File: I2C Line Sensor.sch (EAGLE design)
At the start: 28 parts, among them U1 ADS7830

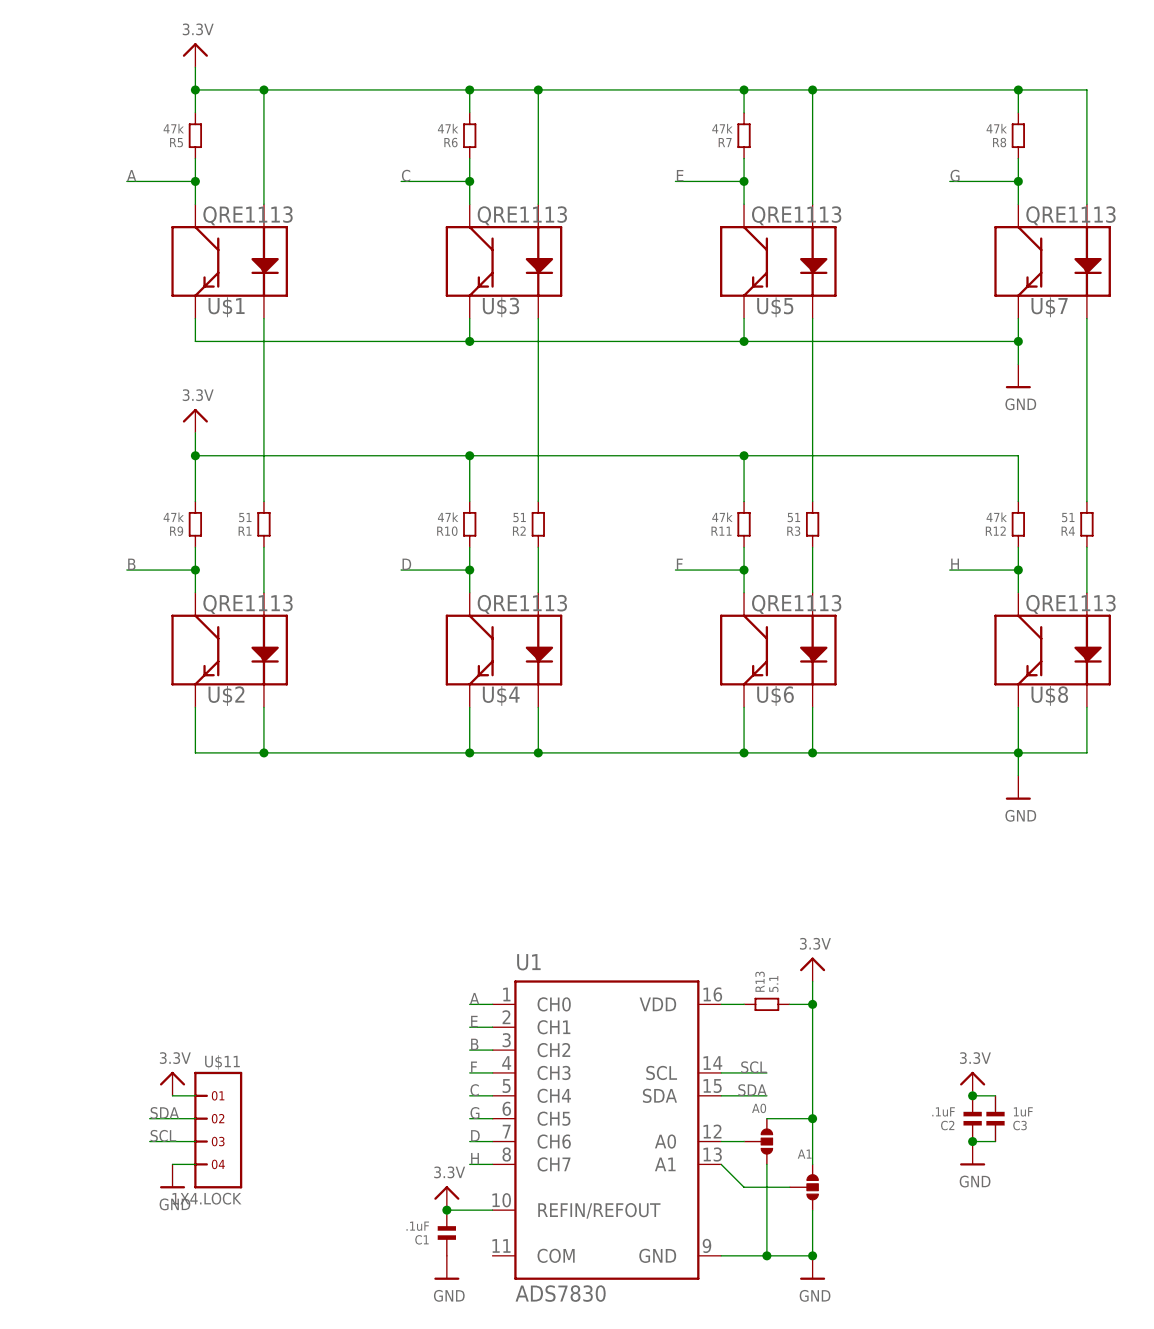
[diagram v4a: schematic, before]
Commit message: Modified resistor values such that the PCBs should no longer get hot
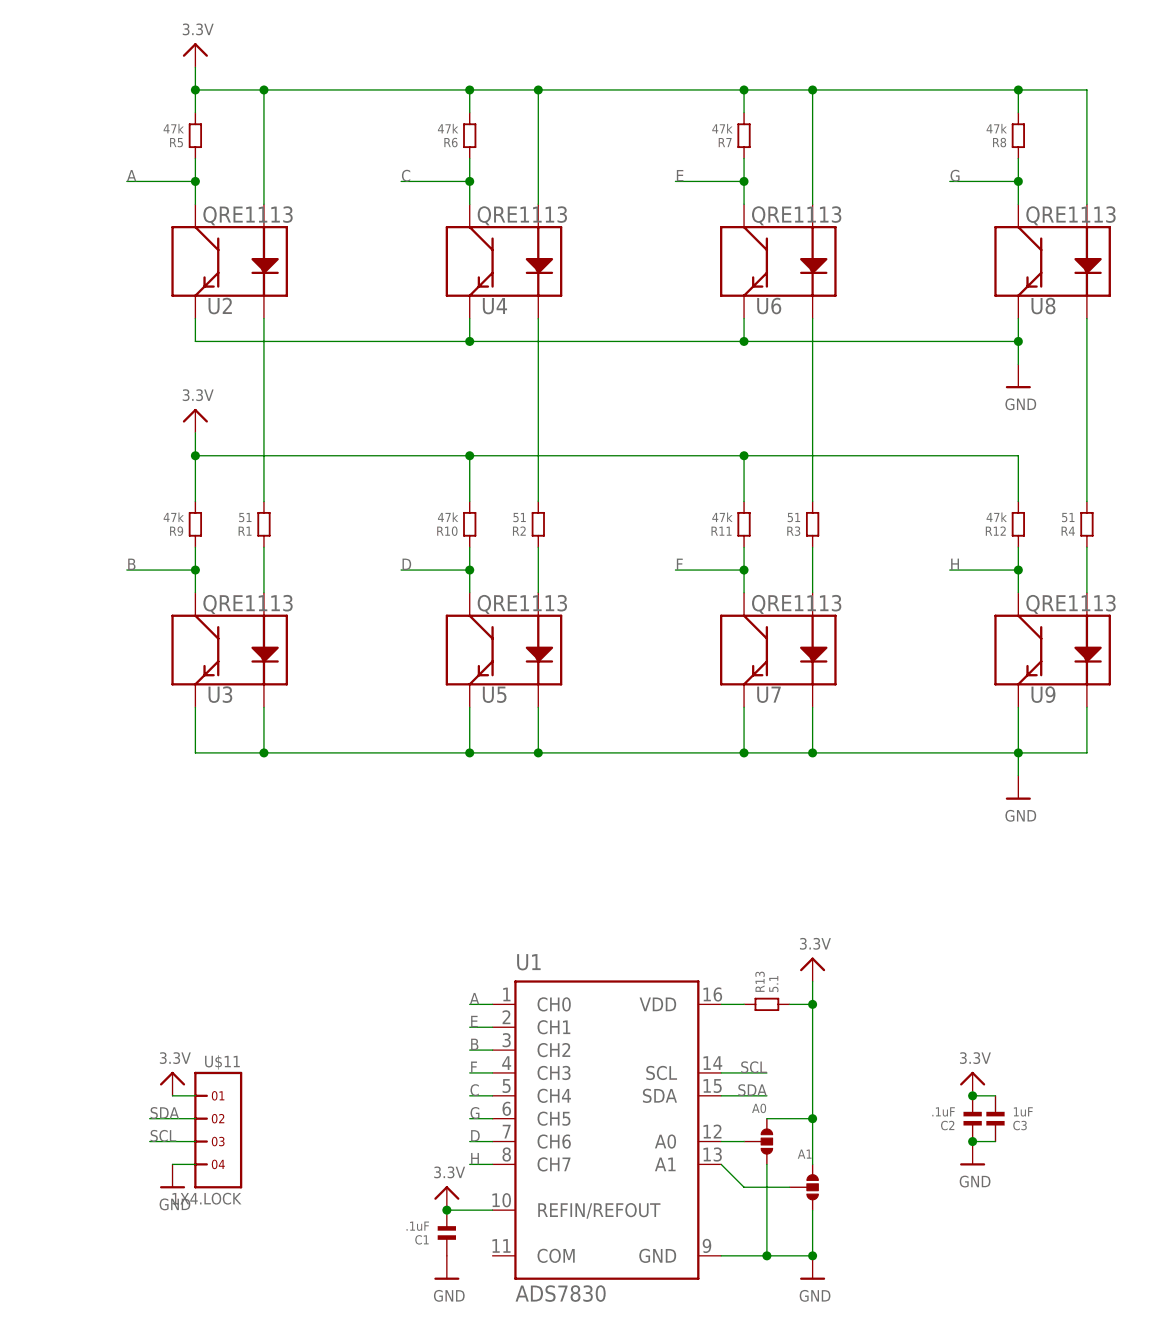
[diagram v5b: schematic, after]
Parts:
- renumbered U$1 to U2, U$2 to U3, U$3 to U4, U$4 to U5, U$5 to U6, U$6 to U7, U$7 to U8, U$8 to U9
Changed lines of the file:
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@@
 </classes>
 <parts>
-<part name="U$1" library="SparkFun" deviceset="QRE1113" device=""/>
-<part name="U$2" library="SparkFun" deviceset="QRE1113" device=""/>
-<part name="U$3" library="SparkFun" deviceset="QRE1113" device=""/>
-<part name="U$4" library="SparkFun" deviceset="QRE1113" device=""/>
-<part name="U$5" library="SparkFun" deviceset="QRE1113" device=""/>
-<part name="U$6" library="SparkFun" deviceset="QRE1113" device=""/>
-<part name="U$7" library="SparkFun" deviceset="QRE1113" device=""/>
-<part name="U$8" library="SparkFun" deviceset="QRE1113" device=""/>
+<part name="U2" library="SparkFun" deviceset="QRE1113" device=""/>
+<part name="U3" library="SparkFun" deviceset="QRE1113" device=""/>
+<part name="U4" library="SparkFun" deviceset="QRE1113" device=""/>
+<part name="U5" library="SparkFun" deviceset="QRE1113" device=""/>
+<part name="U6" library="SparkFun" deviceset="QRE1113" device=""/>
+<part name="U7" library="SparkFun" deviceset="QRE1113" device=""/>
+<part name="U8" library="SparkFun" deviceset="QRE1113" device=""/>
+<part name="U9" library="SparkFun" deviceset="QRE1113" device=""/>
 <part name="U1" library="burr-brown" deviceset="ADS7828" device="" value="ADS7830"/>
 <part name="U$14" library="microbuilder" deviceset="3.3V" device=""/>
@@
 </plain>
 <instances>
-<instance part="U$1" gate="G$1" x="27.94" y="144.78"/>
-<instance part="U$2" gate="G$1" x="27.94" y="101.6"/>
-<instance part="U$3" gate="G$1" x="58.42" y="144.78"/>
-<instance part="U$4" gate="G$1" x="58.42" y="101.6"/>
-<instance part="U$5" gate="G$1" x="88.9" y="144.78"/>
-<instance part="U$6" gate="G$1" x="88.9" y="101.6"/>
-<instance part="U$7" gate="G$1" x="119.38" y="144.78"/>
-<instance part="U$8" gate="G$1" x="119.38" y="101.6"/>
+<instance part="U2" gate="G$1" x="27.94" y="144.78"/>
+<instance part="U3" gate="G$1" x="27.94" y="101.6"/>
+<instance part="U4" gate="G$1" x="58.42" y="144.78"/>
+<instance part="U5" gate="G$1" x="58.42" y="101.6"/>
+<instance part="U6" gate="G$1" x="88.9" y="144.78"/>
+<instance part="U7" gate="G$1" x="88.9" y="101.6"/>
+<instance part="U8" gate="G$1" x="119.38" y="144.78"/>
+<instance part="U9" gate="G$1" x="119.38" y="101.6"/>
 <instance part="U1" gate="G$1" x="71.12" y="48.26"/>
 <instance part="U$14" gate="G$1" x="93.98" y="63.5"/>
@@
 <segment>
 <wire x1="33.02" y1="137.16" x2="33.02" y2="116.84" width="0.1524" layer="91"/>
-<pinref part="U$1" gate="G$1" pin="K"/>
+<pinref part="U2" gate="G$1" pin="K"/>
 <pinref part="R1" gate="G$1" pin="2"/>
 </segment>
@@
 <net name="N$3" class="0">
 <segment>
-<pinref part="U$2" gate="G$1" pin="A"/>
+<pinref part="U3" gate="G$1" pin="A"/>
 <pinref part="R1" gate="G$1" pin="1"/>
 <wire x1="33.02" y1="106.68" x2="33.02" y2="111.76" width="0.1524" layer="91"/>
@@
 <net name="N$4" class="0">
 <segment>
-<pinref part="U$4" gate="G$1" pin="A"/>
+<pinref part="U5" gate="G$1" pin="A"/>
 <pinref part="R2" gate="G$1" pin="1"/>
 <wire x1="63.5" y1="111.76" x2="63.5" y2="106.68" width="0.1524" layer="91"/>
@@
 <segment>
 <wire x1="63.5" y1="137.16" x2="63.5" y2="116.84" width="0.1524" layer="91"/>
-<pinref part="U$3" gate="G$1" pin="K"/>
+<pinref part="U4" gate="G$1" pin="K"/>
 <pinref part="R2" gate="G$1" pin="2"/>
 </segment>
@@
 <segment>
 <wire x1="93.98" y1="137.16" x2="93.98" y2="116.84" width="0.1524" layer="91"/>
-<pinref part="U$5" gate="G$1" pin="K"/>
+<pinref part="U6" gate="G$1" pin="K"/>
 <pinref part="R3" gate="G$1" pin="2"/>
 </segment>
@@
 <net name="N$7" class="0">
 <segment>
-<pinref part="U$6" gate="G$1" pin="A"/>
+<pinref part="U7" gate="G$1" pin="A"/>
 <pinref part="R3" gate="G$1" pin="1"/>
 <wire x1="93.98" y1="111.76" x2="93.98" y2="106.68" width="0.1524" layer="91"/>
@@
 <segment>
 <wire x1="124.46" y1="137.16" x2="124.46" y2="116.84" width="0.1524" layer="91"/>
-<pinref part="U$7" gate="G$1" pin="K"/>
+<pinref part="U8" gate="G$1" pin="K"/>
 <pinref part="R4" gate="G$1" pin="2"/>
 </segment>
@@
 <net name="N$9" class="0">
 <segment>
-<pinref part="U$8" gate="G$1" pin="A"/>
+<pinref part="U9" gate="G$1" pin="A"/>
 <pinref part="R4" gate="G$1" pin="1"/>
 <wire x1="124.46" y1="111.76" x2="124.46" y2="106.68" width="0.1524" layer="91"/>
@@
 <junction x="86.36" y="88.9"/>
 <junction x="116.84" y="88.9"/>
-<pinref part="U$2" gate="G$1" pin="K"/>
-<pinref part="U$8" gate="G$1" pin="K"/>
-<pinref part="U$4" gate="G$1" pin="K"/>
-<pinref part="U$6" gate="G$1" pin="K"/>
-<pinref part="U$4" gate="G$1" pin="E"/>
-<pinref part="U$6" gate="G$1" pin="E"/>
-<pinref part="U$2" gate="G$1" pin="E"/>
-<pinref part="U$8" gate="G$1" pin="E"/>
+<pinref part="U3" gate="G$1" pin="K"/>
+<pinref part="U9" gate="G$1" pin="K"/>
+<pinref part="U5" gate="G$1" pin="K"/>
+<pinref part="U7" gate="G$1" pin="K"/>
+<pinref part="U5" gate="G$1" pin="E"/>
+<pinref part="U7" gate="G$1" pin="E"/>
+<pinref part="U3" gate="G$1" pin="E"/>
+<pinref part="U9" gate="G$1" pin="E"/>
 <pinref part="U$22" gate="G$1" pin="GND"/>
 <wire x1="116.84" y1="86.36" x2="116.84" y2="88.9" width="0.1524" layer="91"/>
 </segment>
 <segment>
-<pinref part="U$7" gate="G$1" pin="E"/>
+<pinref part="U8" gate="G$1" pin="E"/>
 <wire x1="116.84" y1="134.62" x2="116.84" y2="137.16" width="0.1524" layer="91"/>
-<pinref part="U$5" gate="G$1" pin="E"/>
+<pinref part="U6" gate="G$1" pin="E"/>
 <wire x1="86.36" y1="134.62" x2="86.36" y2="137.16" width="0.1524" layer="91"/>
 <wire x1="86.36" y1="134.62" x2="116.84" y2="134.62" width="0.1524" layer="91"/>
 <junction x="86.36" y="134.62"/>
 <wire x1="55.88" y1="134.62" x2="86.36" y2="134.62" width="0.1524" layer="91"/>
-<pinref part="U$3" gate="G$1" pin="E"/>
+<pinref part="U4" gate="G$1" pin="E"/>
 <wire x1="55.88" y1="137.16" x2="55.88" y2="134.62" width="0.1524" layer="91"/>
 <junction x="55.88" y="134.62"/>
-<pinref part="U$1" gate="G$1" pin="E"/>
+<pinref part="U2" gate="G$1" pin="E"/>
 <wire x1="25.4" y1="137.16" x2="25.4" y2="134.62" width="0.1524" layer="91"/>
 <wire x1="25.4" y1="134.62" x2="55.88" y2="134.62" width="0.1524" layer="91"/>
@@
 <wire x1="25.4" y1="152.4" x2="25.4" y2="149.86" width="0.1524" layer="91"/>
 <wire x1="25.4" y1="152.4" x2="17.78" y2="152.4" width="0.1524" layer="91"/>
-<pinref part="U$1" gate="G$1" pin="C"/>
+<pinref part="U2" gate="G$1" pin="C"/>
 <pinref part="R5" gate="G$1" pin="1"/>
 <wire x1="25.4" y1="154.94" x2="25.4" y2="152.4" width="0.1524" layer="91"/>
@@
 <wire x1="25.4" y1="109.22" x2="25.4" y2="106.68" width="0.1524" layer="91"/>
 <wire x1="25.4" y1="109.22" x2="17.78" y2="109.22" width="0.1524" layer="91"/>
-<pinref part="U$2" gate="G$1" pin="C"/>
+<pinref part="U3" gate="G$1" pin="C"/>
 <pinref part="R9" gate="G$1" pin="1"/>
 <wire x1="25.4" y1="111.76" x2="25.4" y2="109.22" width="0.1524" layer="91"/>
@@
 <wire x1="55.88" y1="152.4" x2="55.88" y2="149.86" width="0.1524" layer="91"/>
 <wire x1="55.88" y1="152.4" x2="48.26" y2="152.4" width="0.1524" layer="91"/>
-<pinref part="U$3" gate="G$1" pin="C"/>
+<pinref part="U4" gate="G$1" pin="C"/>
 <pinref part="R6" gate="G$1" pin="1"/>
 <wire x1="55.88" y1="152.4" x2="55.88" y2="154.94" width="0.1524" layer="91"/>
@@
 <wire x1="55.88" y1="109.22" x2="55.88" y2="106.68" width="0.1524" layer="91"/>
 <wire x1="55.88" y1="109.22" x2="48.26" y2="109.22" width="0.1524" layer="91"/>
-<pinref part="U$4" gate="G$1" pin="C"/>
+<pinref part="U5" gate="G$1" pin="C"/>
 <pinref part="R10" gate="G$1" pin="1"/>
 <wire x1="55.88" y1="109.22" x2="55.88" y2="111.76" width="0.1524" layer="91"/>
@@
 <wire x1="86.36" y1="152.4" x2="86.36" y2="149.86" width="0.1524" layer="91"/>
 <wire x1="86.36" y1="152.4" x2="78.74" y2="152.4" width="0.1524" layer="91"/>
-<pinref part="U$5" gate="G$1" pin="C"/>
+<pinref part="U6" gate="G$1" pin="C"/>
 <pinref part="R7" gate="G$1" pin="1"/>
 <wire x1="86.36" y1="154.94" x2="86.36" y2="152.4" width="0.1524" layer="91"/>
@@
 <wire x1="86.36" y1="109.22" x2="86.36" y2="106.68" width="0.1524" layer="91"/>
 <wire x1="86.36" y1="109.22" x2="78.74" y2="109.22" width="0.1524" layer="91"/>
-<pinref part="U$6" gate="G$1" pin="C"/>
+<pinref part="U7" gate="G$1" pin="C"/>
 <pinref part="R11" gate="G$1" pin="1"/>
 <wire x1="86.36" y1="111.76" x2="86.36" y2="109.22" width="0.1524" layer="91"/>
@@
 <wire x1="116.84" y1="152.4" x2="116.84" y2="149.86" width="0.1524" layer="91"/>
 <wire x1="116.84" y1="152.4" x2="109.22" y2="152.4" width="0.1524" layer="91"/>
-<pinref part="U$7" gate="G$1" pin="C"/>
+<pinref part="U8" gate="G$1" pin="C"/>
 <pinref part="R8" gate="G$1" pin="1"/>
 <wire x1="116.84" y1="152.4" x2="116.84" y2="154.94" width="0.1524" layer="91"/>
@@
 <wire x1="116.84" y1="109.22" x2="116.84" y2="106.68" width="0.1524" layer="91"/>
 <wire x1="116.84" y1="109.22" x2="109.22" y2="109.22" width="0.1524" layer="91"/>
-<pinref part="U$8" gate="G$1" pin="C"/>
+<pinref part="U9" gate="G$1" pin="C"/>
 <pinref part="R12" gate="G$1" pin="1"/>
 <wire x1="116.84" y1="111.76" x2="116.84" y2="109.22" width="0.1524" layer="91"/>
@@
 <junction x="63.5" y="162.56"/>
 <junction x="93.98" y="162.56"/>
-<pinref part="U$1" gate="G$1" pin="A"/>
-<pinref part="U$3" gate="G$1" pin="A"/>
-<pinref part="U$5" gate="G$1" pin="A"/>
-<pinref part="U$7" gate="G$1" pin="A"/>
+<pinref part="U2" gate="G$1" pin="A"/>
+<pinref part="U4" gate="G$1" pin="A"/>
+<pinref part="U6" gate="G$1" pin="A"/>
+<pinref part="U8" gate="G$1" pin="A"/>
 <pinref part="R5" gate="G$1" pin="2"/>
 <wire x1="25.4" y1="162.56" x2="25.4" y2="160.02" width="0.1524" layer="91"/>
